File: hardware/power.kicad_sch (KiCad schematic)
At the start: 96 parts, among them J3 Vcore_sel, U1 TLV62569DBV, U2 TLV62569DBV, U3 MPM3833CGRH-Z, U4 CCGM1A1, U5 TLV62569DBV, U6 TLV62569DBV

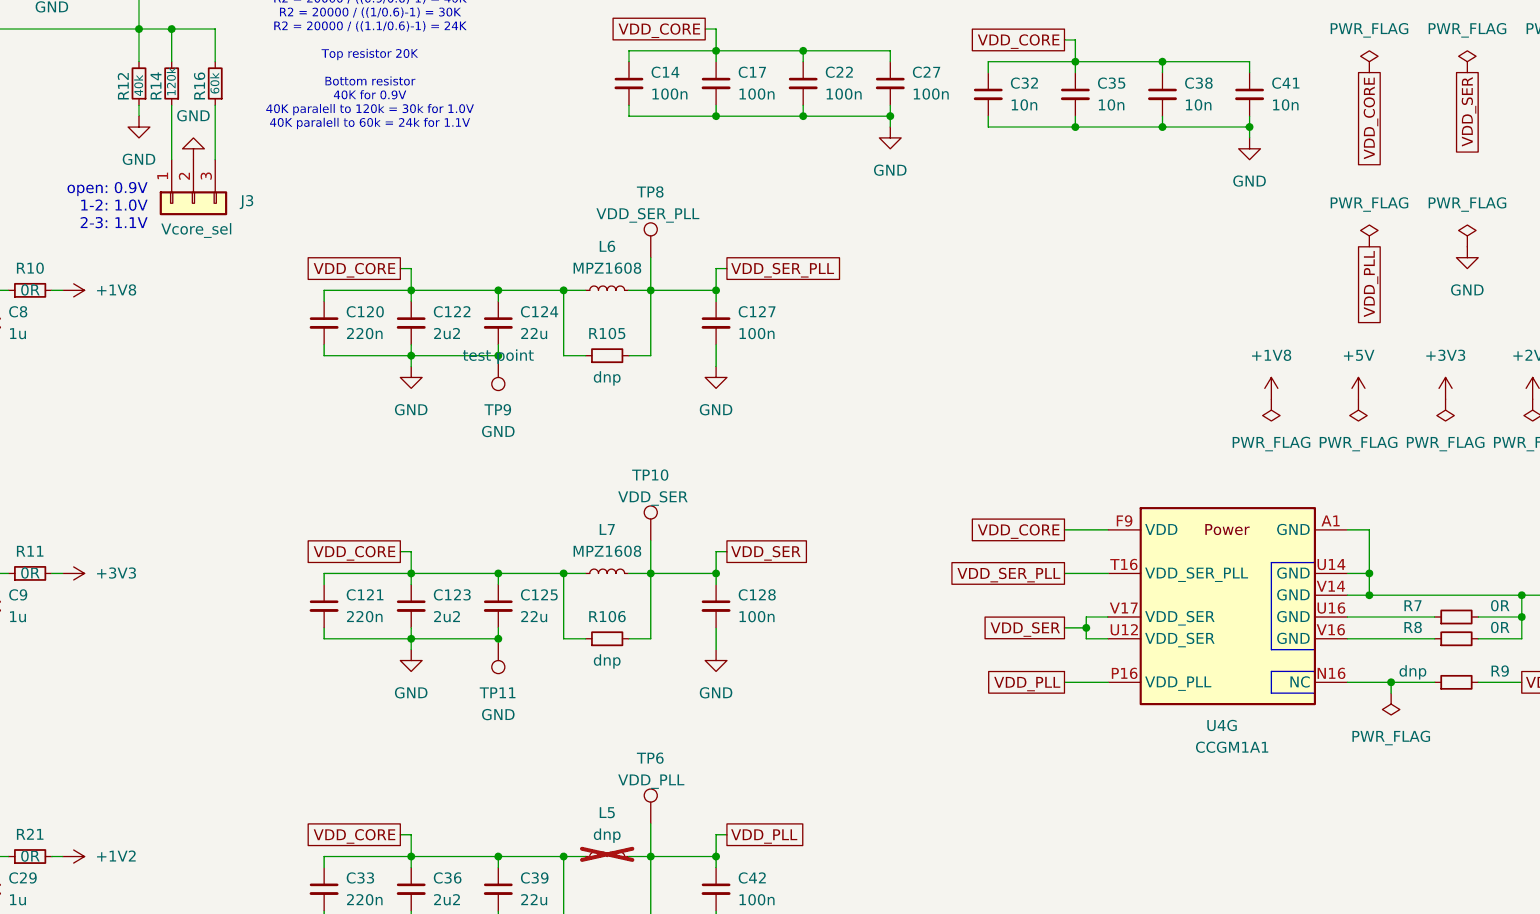
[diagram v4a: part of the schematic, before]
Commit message: Connecting PWR and FAN_PWM to NC pins, using NC3 for Ethernet clock
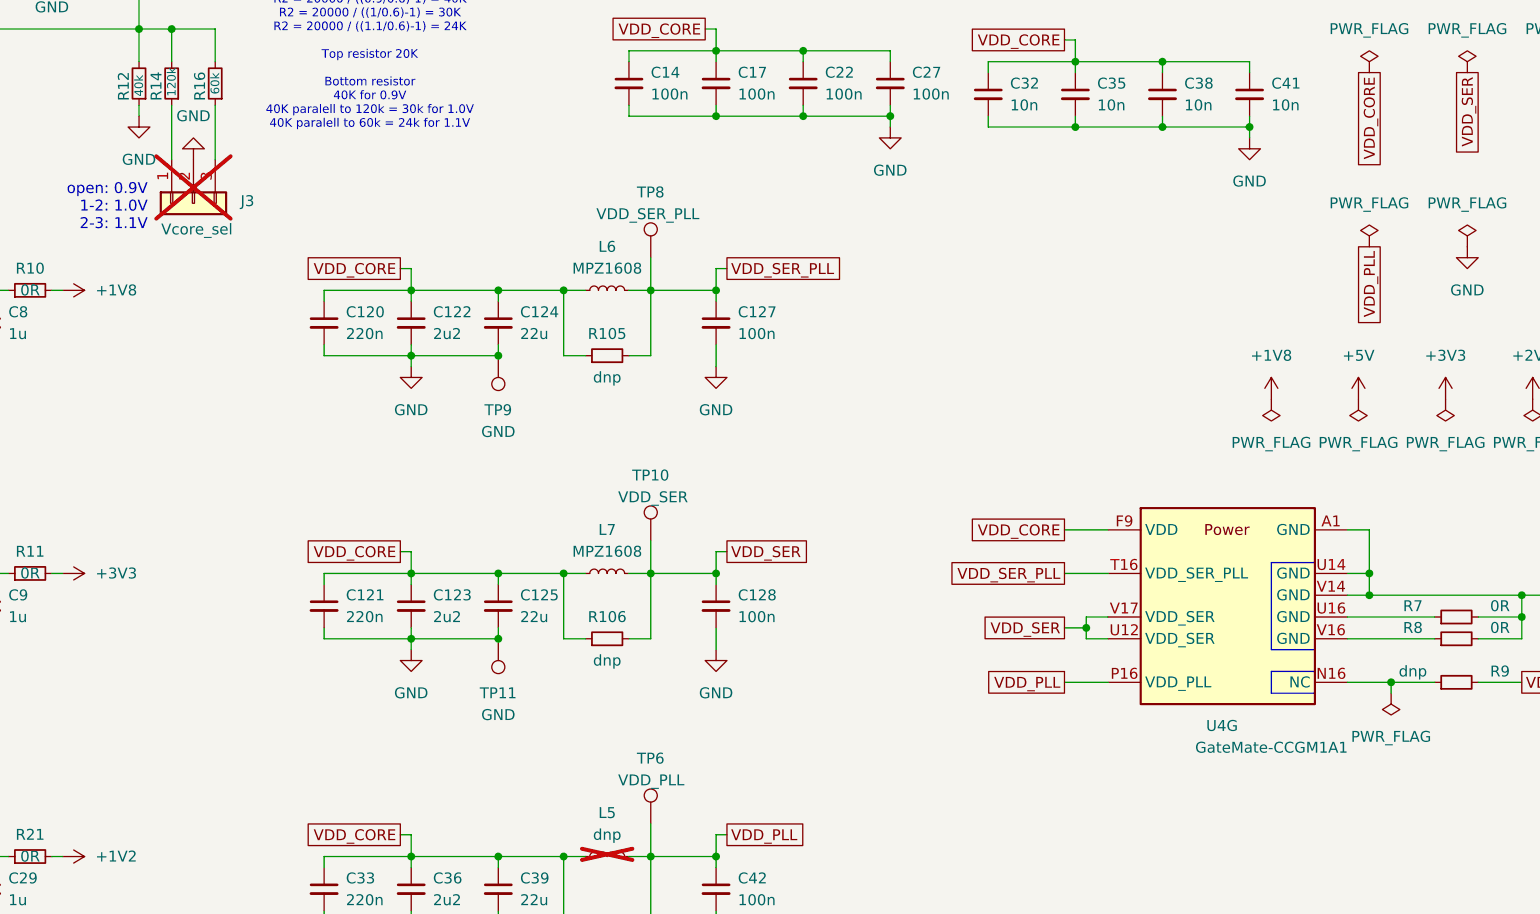
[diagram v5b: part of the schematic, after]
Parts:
- J3: now not fitted; now left out of the parts list
- TP1, TP10, TP11, TP2, TP3, TP4, TP5, TP6, TP7, TP8, TP9: now left out of the parts list
- U4: value CCGM1A1 -> GateMate-CCGM1A1
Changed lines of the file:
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@@
 		(unit 1)
 		(exclude_from_sim no)
-		(in_bom yes)
+		(in_bom no)
 		(on_board yes)
 		(dnp no)
@@
 		(unit 1)
 		(exclude_from_sim no)
-		(in_bom yes)
+		(in_bom no)
 		(on_board yes)
 		(dnp no)
@@
 		(unit 1)
 		(exclude_from_sim no)
-		(in_bom yes)
+		(in_bom no)
 		(on_board yes)
 		(dnp no)
@@
 		(unit 1)
 		(exclude_from_sim no)
-		(in_bom yes)
+		(in_bom no)
 		(on_board yes)
 		(dnp no)
@@
 		(unit 1)
 		(exclude_from_sim no)
-		(in_bom yes)
+		(in_bom no)
 		(on_board yes)
 		(dnp no)
@@
 		(unit 1)
 		(exclude_from_sim no)
-		(in_bom yes)
+		(in_bom no)
 		(on_board yes)
 		(dnp no)
@@
 		(unit 1)
 		(exclude_from_sim no)
-		(in_bom yes)
+		(in_bom no)
 		(on_board yes)
 		(dnp no)
@@
 		(unit 1)
 		(exclude_from_sim no)
-		(in_bom yes)
+		(in_bom no)
 		(on_board yes)
 		(dnp no)
@@
 		(unit 1)
 		(exclude_from_sim no)
-		(in_bom yes)
+		(in_bom no)
 		(on_board yes)
 		(dnp no)
@@
 		(unit 1)
 		(exclude_from_sim no)
-		(in_bom yes)
+		(in_bom no)
 		(on_board yes)
 		(dnp no)
@@
 		)
 		(property "Description" "test point"
-			(at 148.59 83.82 0)
+			(at 150.622 88.646 0)
 			(effects
 				(font
 					(size 1.27 1.27)
 				)
+				(hide yes)
 			)
 		)
@@
 		(unit 1)
 		(exclude_from_sim no)
-		(in_bom yes)
+		(in_bom no)
 		(on_board yes)
-		(dnp no)
+		(dnp yes)
 		(property "Reference" "J3"
 			(at 120.142 65.786 90)
@@
 			)
 		)
-		(property "Value" "CCGM1A1"
+		(property "Value" "GateMate-CCGM1A1"
 			(at 229.87 129.54 0)
 			(effects
@@
 		(unit 1)
 		(exclude_from_sim no)
-		(in_bom yes)
+		(in_bom no)
 		(on_board yes)
 		(dnp no)

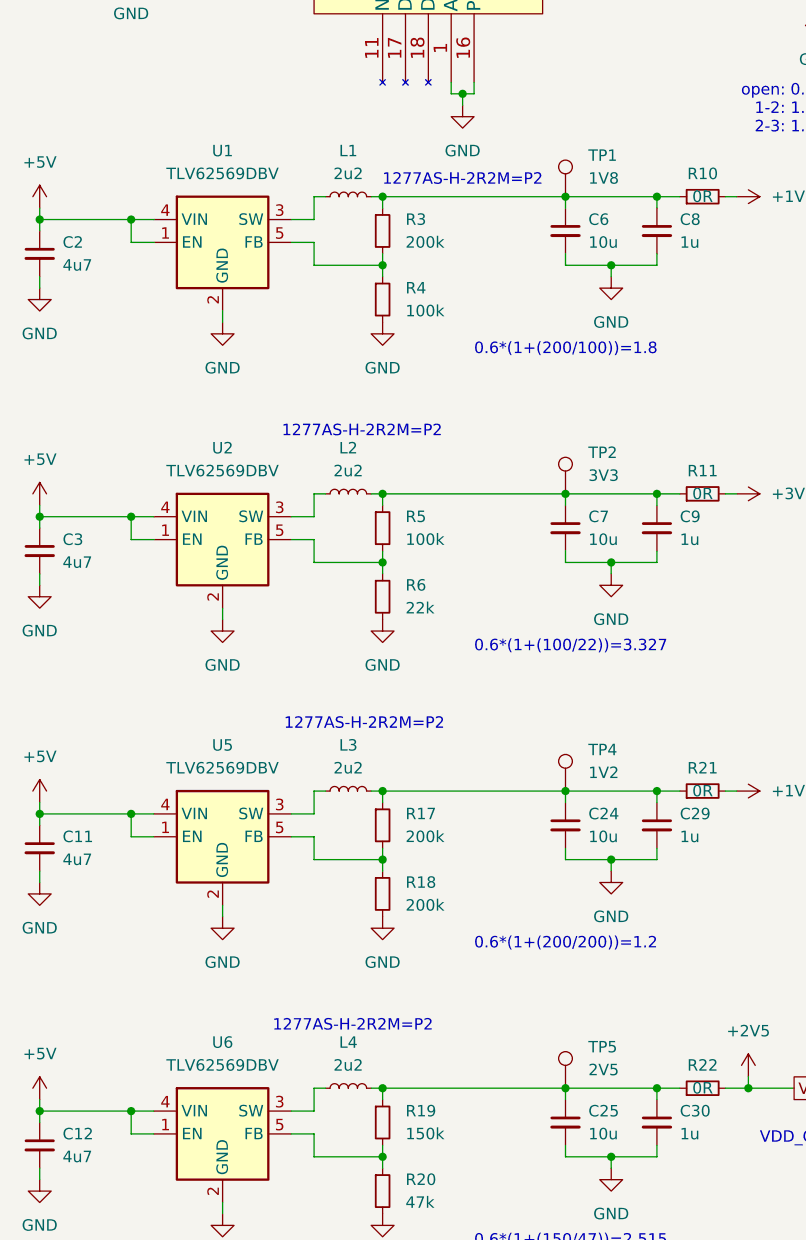
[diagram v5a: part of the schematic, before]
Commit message: Updating sch - moving power select resistors to bottom
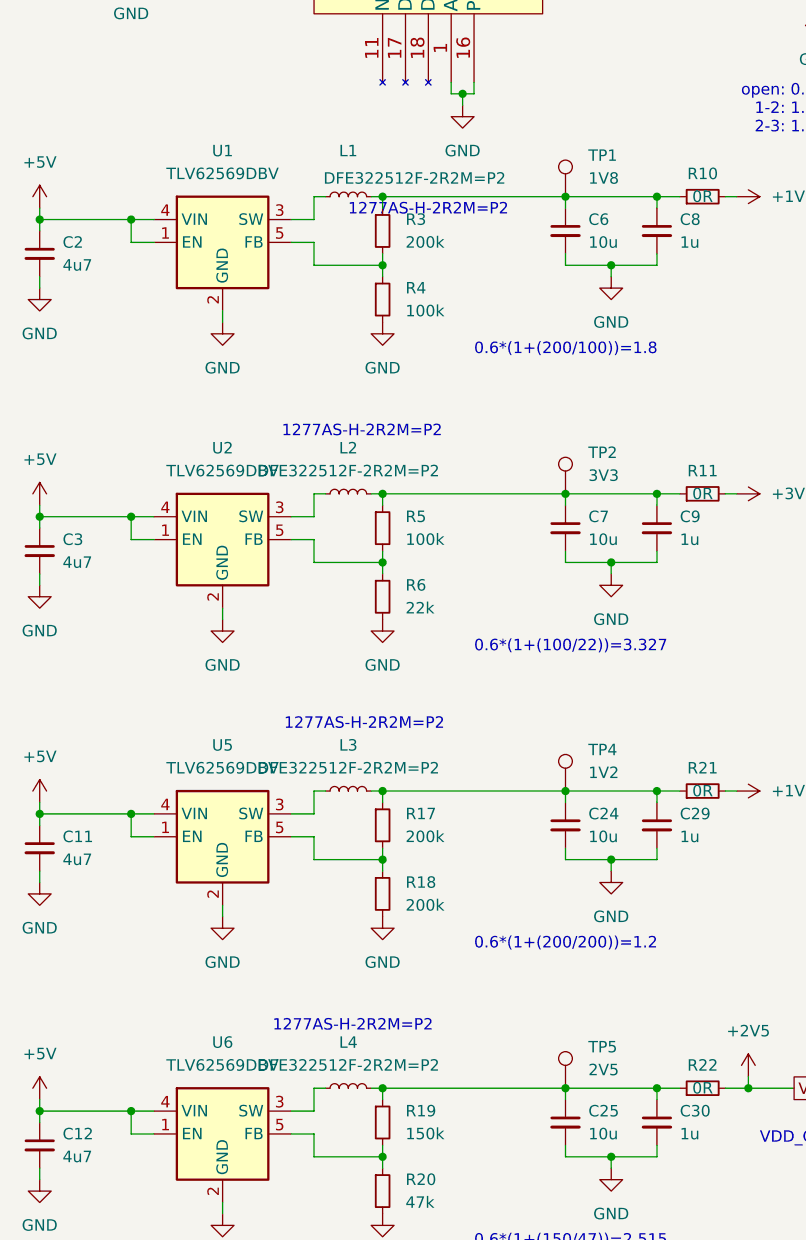
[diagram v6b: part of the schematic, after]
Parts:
- L1, L2, L3, L4: value 2u2 -> DFE322512F-2R2M=P2
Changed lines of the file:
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@@
 	(text "1277AS-H-2R2M=P2"
 		(exclude_from_sim no)
-		(at 67.31 74.422 0)
+		(at 63.5 77.724 0)
 		(effects
 			(font
@@
 			)
 		)
-		(property "Value" "2u2"
+		(property "Value" "DFE322512F-2R2M=P2"
 			(at 54.61 172.72 90)
 			(effects
@@
 			)
 		)
-		(property "Value" "2u2"
+		(property "Value" "DFE322512F-2R2M=P2"
 			(at 54.61 106.68 90)
 			(effects
@@
 		(on_board yes)
 		(dnp no)
-		(fields_autoplaced yes)
 		(property "Reference" "L1"
 			(at 54.61 71.12 90)
@@
 			)
 		)
-		(property "Value" "2u2"
-			(at 54.61 73.66 90)
+		(property "Value" "DFE322512F-2R2M=P2"
+			(at 61.976 74.168 90)
 			(effects
 				(font
@@
 			)
 		)
-		(property "Value" "2u2"
+		(property "Value" "DFE322512F-2R2M=P2"
 			(at 54.61 139.7 90)
 			(effects

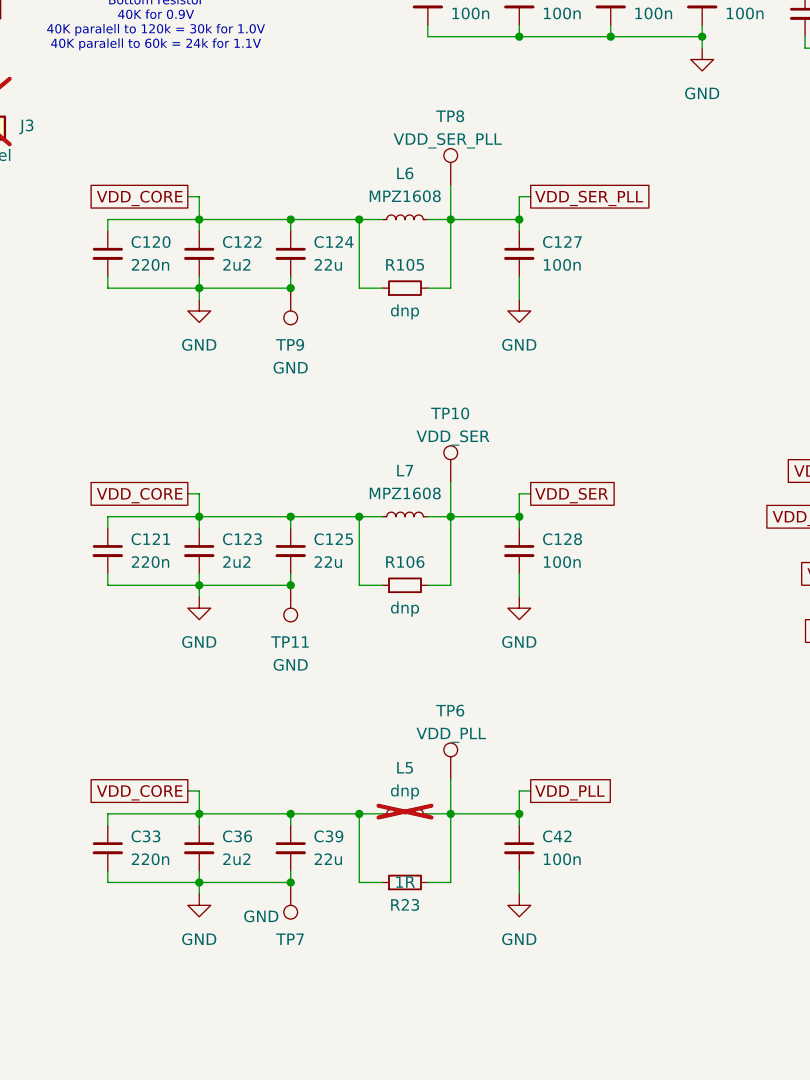
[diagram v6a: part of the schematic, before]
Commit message: Fix #23 added DNP to L, R changed to 1R, All power resistors moved to 0603
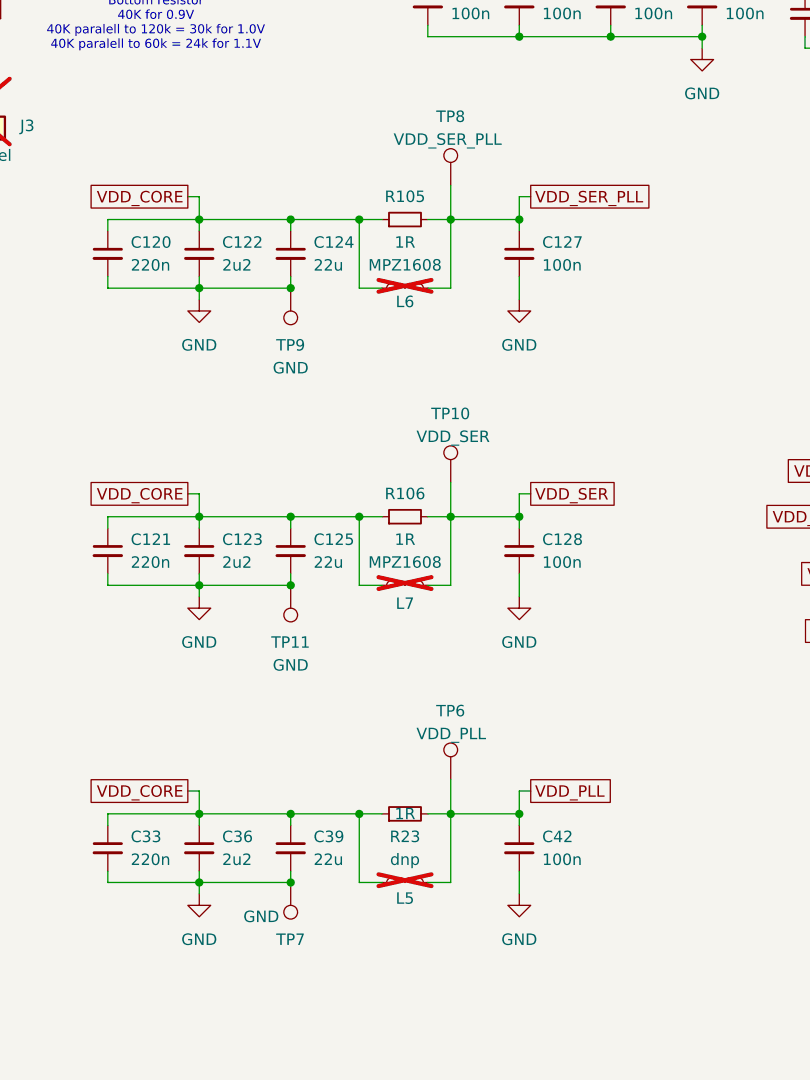
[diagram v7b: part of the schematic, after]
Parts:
- L6, L7: now not fitted; now left out of the parts list
- R10, R11, R13, R21, R22, R23: footprint Resistor_SMD:R_0402_1005Metric -> Resistor_SMD:R_0603_1608Metric
- R105, R106: value dnp -> 1R; footprint Resistor_SMD:R_0402_1005Metric -> Resistor_SMD:R_0603_1608Metric
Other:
- moved on the sheet: L5, R105, R106, R23
